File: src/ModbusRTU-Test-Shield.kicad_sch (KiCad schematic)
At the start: 23 parts, among them J1 Conn_01x08_UNO_Digital_1, J2 Conn_01x10_UNO_Digital_2, J3 Conn_01x08_UNO_Power, J4 Conn_01x06_UNO_Analog, J5 Screw_Terminal_01x03, SW1 SW_Push, SW2 SW_Push, SW3 SW_Push, SW4 SW_DPDT_x2, U1 LT1785AxN8

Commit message: Completed first draft.
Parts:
- removed R6: 2K, Resistor_THT:R_Axial_DIN0207_L6.3mm_D2.5mm_P10.16mm_Horizontal, symbol Device:R
- added D5: YEL, LED_THT:LED_D3.0mm, symbol Device:LED
- added R5: 330, Resistor_THT:R_Axial_DIN0207_L6.3mm_D2.5mm_P10.16mm_Horizontal, symbol Device:R
- added R7: 2K, Resistor_THT:R_Axial_DIN0207_L6.3mm_D2.5mm_P10.16mm_Horizontal, symbol Device:R
- renumbered R5 to R6
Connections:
- net *5: now also R1.1; no longer D1.2 (A)
- net *6: now also R2.1; no longer D2.2 (A)
- net 13: now also R5.1
- net 7: now also R3.1; no longer D3.2 (A)
- net 8: now also R4.1; no longer D4.2 (A)
- net GND: now also D1.1 (K), D2.1 (K), D3.1 (K), D4.1 (K), D5.1 (K), R7.2; no longer R1.2, R2.2, R3.2, R4.2
- net at R6.2, SW4.5 (B): now also R7.1
- new net: D1.2 (A), R1.2
- new net: D4.2 (A), R4.2
- new net: D2.2 (A), R2.2
- new net: D5.2 (A), R5.2
- new net: D3.2 (A), R3.2
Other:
- moved on the sheet: C1, D1, D2, D3, D4, J1, J2, J3, J4, J5, R1, R2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

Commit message: Added RS-232 on an RJ12 connector. Completed second draft.
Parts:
- added C2, C3, C4, C5, C6: 1uF, Capacitor_THT:CP_Radial_D5.0mm_P2.50mm, symbol Device:C_Polarized_Small
- added D10, D9: YEL, LED_THT:LED_D3.0mm, symbol Device:LED
- added D11: D_Schottky, Diode_THT:D_DO-41_SOD81_P10.16mm_Horizontal, symbol Device:D_Schottky
- added D6, D7: D_Schottky, Diode_THT:D_DO-35_SOD27_P7.62mm_Horizontal, symbol Device:D_Schottky
- added D8: GRN, LED_THT:LED_D3.0mm, symbol Device:LED
- added J6: 6P6C, Connector_RJ:RJ12_Amphenol_54601, symbol Connector:6P6C
- added R8, R9: 330, Resistor_THT:R_Axial_DIN0207_L6.3mm_D2.5mm_P10.16mm_Horizontal, symbol Device:R
- added U2: MAX232, Package_DIP:DIP-16_W7.62mm, symbol Interface_UART:MAX232
- R6: value 1K -> 10K
- R7: value 2K -> 330
- SW1: value SW_Push -> RESET; footprint Button_Switch_THT:SW_PUSH_6mm -> Project_Footprints:SW_PUSH_6mm_Reset
- SW2: value SW_Push -> BUTTON1
- SW3: value SW_Push -> BUTTON2
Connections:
- net +5V: now also C6.1, D11.1 (K), D8.2 (A), J6.2, U2.16 (VCC)
- net GND: now also C4.2, C5.1, C6.2, J6.1, J6.6, U2.15 (GND)
- net IOREF: now also R6.1, D10.2 (A), D9.2 (A)
- net at U1.1 (RO): now also D6.1 (K); no longer R6.1
- net RX: now reaches SW4.2 (B)
- net RX: now also R6.2, D6.2 (A), D7.2 (A), R9.2; no longer U1.4 (DI)
- net RS485_D+: now reaches J5.1 (Pin_1), U1.6 (A)
- net RS485_D-: now reaches J5.2 (Pin_2), U1.7 (B)
- net RESET: now reaches J3.3 (RESET), SW1.1
- net *10 renamed SOFT_RX
- net SOFT_RX: now also SW4.3 (C); no longer SW4.6 (C)
- net *11 renamed SOFT_TX
- net SOFT_TX: now also SW4.6 (C); no longer SW4.3 (C)
- net *3 renamed BUTTON1
- net *5 renamed LED4
- net *6 renamed LED3
- net 13 renamed DE
- net 2 renamed BUTTON2
- net 7 renamed LED2
- net 8 renamed LED1
- net A0 renamed POT1
- net A1 renamed POT2
- net RX/0 renamed HARD_RX
- net HARD_RX: now also SW4.1 (A); no longer SW4.4 (A)
- net TX/1 renamed HARD_TX
- net HARD_TX: now also SW4.4 (A); no longer SW4.1 (A)
- new net: D10.1 (K), R9.1
- new net: C3.1, U2.1 (C1+)
- new net: C3.2, U2.3 (C1-)
- new net: D9.1 (K), R8.1
- new net: C5.2, U2.6 (VS-)
- new net: D8.1 (K), R7.1
- new net: D11.2 (A), J6.5
- new net: D7.1 (K), U2.12 (R1OUT)
- new net: C4.1, U2.2 (VS+)
- new net: C2.1, U2.4 (C2+)
- new net: C2.2, U2.5 (C2-)
- new net RS232_RX: J6.3, U2.13 (R1IN)
- new net RS232_TX: J6.4, U2.14 (T1OUT)
- new net TX: R8.2, SW4.5 (B), U1.4 (DI), U2.11 (T1IN)
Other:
- note removed: "* Indicates a PWM-capable pin"
- moved on the sheet: C1, D5, J5, R5, RV1, RV2, SW1, SW2, SW3

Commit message: Added some 3D models. Created project footprints for RJ12 and screw terminal connectors. Placed and locked RJ12 and screw terminal connector.
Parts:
- J5: footprint Connector_Phoenix_MC:PhoenixContact_MC_1,5_3-G-3.5_1x03_P3.50mm_Horizontal -> Project_Footprints:PhoenixContact_BCH-350H-3_RS485; Manufacturer (none) -> Phoenix Contact; Part Number (none) -> 5430438
- J6: footprint Connector_RJ:RJ12_Amphenol_54601 -> Project_Footprints:FCI_54601-906WPLF; Manufacturer (none) -> Amphenol ICC (FCI); Part Number (none) -> 54601-906WPLF
- R1, R2, R3, R4, R5, R6, R7, R8, R9: footprint Resistor_THT:R_Axial_DIN0207_L6.3mm_D2.5mm_P10.16mm_Horizontal -> Resistor_THT:R_Axial_DIN0204_L3.6mm_D1.6mm_P7.62mm_Horizontal
- U1: footprint Package_DIP:DIP-8_W7.62mm -> Package_DIP:DIP-8_W7.62mm_Socket
- U2: footprint Package_DIP:DIP-16_W7.62mm -> Package_DIP:DIP-16_W7.62mm_Socket
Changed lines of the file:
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@@
       (effects (font (size 1.27 1.27)) (justify left))
     )
-    (property "Footprint" "Resistor_THT:R_Axial_DIN0207_L6.3mm_D2.5mm_P10.16mm_Horizontal" (at 430.022 105.41 90)
+    (property "Footprint" "Resistor_THT:R_Axial_DIN0204_L3.6mm_D1.6mm_P7.62mm_Horizontal" (at 430.022 105.41 90)
       (effects (font (size 1.27 1.27)) hide)
     )
@@
       (effects (font (size 1.27 1.27)) (justify left))
     )
-    (property "Footprint" "Package_DIP:DIP-8_W7.62mm" (at 165.1 182.88 0)
+    (property "Footprint" "Package_DIP:DIP-8_W7.62mm_Socket" (at 165.1 182.88 0)
       (effects (font (size 1.27 1.27)) hide)
     )
     (property "Datasheet" "https://www.analog.com/media/en/technical-documentation/data-sheets/LT1785-1785A-1791-1791A.pdf" (at 177.8 157.48 0)
+      (effects (font (size 1.27 1.27)) hide)
+    )
+    (property "Manufacturer" "" (at 165.1 160.02 0)
+      (effects (font (size 1.27 1.27)) hide)
+    )
+    (property "Part Number" "" (at 165.1 160.02 0)
+      (effects (font (size 1.27 1.27)) hide)
+    )
+    (property "Description" "" (at 165.1 160.02 0)
+      (effects (font (size 1.27 1.27)) hide)
+    )
+    (property "Item" "" (at 165.1 160.02 0)
       (effects (font (size 1.27 1.27)) hide)
     )
@@
       (effects (font (size 1.27 1.27)) (justify left))
     )
-    (property "Footprint" "Resistor_THT:R_Axial_DIN0207_L6.3mm_D2.5mm_P10.16mm_Horizontal" (at 417.322 105.41 90)
+    (property "Footprint" "Resistor_THT:R_Axial_DIN0204_L3.6mm_D1.6mm_P7.62mm_Horizontal" (at 417.322 105.41 90)
       (effects (font (size 1.27 1.27)) hide)
     )
@@
       (effects (font (size 1.27 1.27)) (justify left))
     )
-    (property "Footprint" "Resistor_THT:R_Axial_DIN0207_L6.3mm_D2.5mm_P10.16mm_Horizontal" (at 353.822 95.25 90)
+    (property "Footprint" "Resistor_THT:R_Axial_DIN0204_L3.6mm_D1.6mm_P7.62mm_Horizontal" (at 353.822 95.25 90)
       (effects (font (size 1.27 1.27)) hide)
     )
@@
       (effects (font (size 1.27 1.27)) (justify left))
     )
-    (property "Footprint" "Resistor_THT:R_Axial_DIN0207_L6.3mm_D2.5mm_P10.16mm_Horizontal" (at 341.122 95.25 90)
+    (property "Footprint" "Resistor_THT:R_Axial_DIN0204_L3.6mm_D1.6mm_P7.62mm_Horizontal" (at 341.122 95.25 90)
       (effects (font (size 1.27 1.27)) hide)
     )
@@
       (effects (font (size 1.27 1.27)) (justify left))
     )
-    (property "Footprint" "Connector_Phoenix_MC:PhoenixContact_MC_1,5_3-G-3.5_1x03_P3.50mm_Horizontal" (at 106.68 154.94 0)
-      (effects (font (size 1.27 1.27)) hide)
-    )
-    (property "Datasheet" "~" (at 106.68 154.94 0)
+    (property "Footprint" "Project_Footprints:PhoenixContact_BCH-350H-3_RS485" (at 106.68 154.94 0)
+      (effects (font (size 1.27 1.27)) hide)
+    )
+    (property "Datasheet" "https://pxc-crisp-production-platform-cr-s3downloadbucket-1rf23da6xdlmt.s3.eu-west-1.amazonaws.com/8023209?response-content-disposition=inline%3B%20filename%3D%22pxc_5430438_01_01_BCH-350H-3-GY_FAM.pdf%22&X-Amz-Algorithm=AWS4-HMAC-SHA256&X-Amz-Date=20231214T042124Z&X-Amz-SignedHeaders=host&X-Amz-Expires=10800&X-Amz-Credential=AKIAWWXX4BDRFPQUJUER%2F20231214%2Feu-west-1%2Fs3%2Faws4_request&X-Amz-Signature=642cf48a3280ba600a0d77ac701bfd69076ef8d12d5102349e7adfa4ea6ee9f3" (at 106.68 154.94 0)
+      (effects (font (size 1.27 1.27)) hide)
+    )
+    (property "Manufacturer" "Phoenix Contact" (at 106.68 154.94 0)
+      (effects (font (size 1.27 1.27)) hide)
+    )
+    (property "Part Number" "5430438" (at 106.68 154.94 0)
+      (effects (font (size 1.27 1.27)) hide)
+    )
+    (property "Description" "3-Position Terminal Block Header" (at 106.68 154.94 0)
+      (effects (font (size 1.27 1.27)) hide)
+    )
+    (property "Item" "" (at 106.68 154.94 0)
       (effects (font (size 1.27 1.27)) hide)
     )
@@
       (effects (font (size 1.27 1.27)) (justify left))
     )
-    (property "Footprint" "Resistor_THT:R_Axial_DIN0207_L6.3mm_D2.5mm_P10.16mm_Horizontal" (at 404.622 105.41 90)
+    (property "Footprint" "Resistor_THT:R_Axial_DIN0204_L3.6mm_D1.6mm_P7.62mm_Horizontal" (at 404.622 105.41 90)
       (effects (font (size 1.27 1.27)) hide)
     )
@@
       (effects (font (size 1.27 1.27)) (justify left))
     )
-    (property "Footprint" "Resistor_THT:R_Axial_DIN0207_L6.3mm_D2.5mm_P10.16mm_Horizontal" (at 239.522 184.15 90)
+    (property "Footprint" "Resistor_THT:R_Axial_DIN0204_L3.6mm_D1.6mm_P7.62mm_Horizontal" (at 239.522 184.15 90)
       (effects (font (size 1.27 1.27)) hide)
     )
@@
       (effects (font (size 1.27 1.27)) (justify left))
     )
-    (property "Footprint" "Resistor_THT:R_Axial_DIN0207_L6.3mm_D2.5mm_P10.16mm_Horizontal" (at 366.522 95.25 90)
+    (property "Footprint" "Resistor_THT:R_Axial_DIN0204_L3.6mm_D1.6mm_P7.62mm_Horizontal" (at 366.522 95.25 90)
       (effects (font (size 1.27 1.27)) hide)
     )
@@
       (effects (font (size 1.27 1.27)) (justify right))
     )
-    (property "Footprint" "Connector_RJ:RJ12_Amphenol_54601" (at 50.8 221.615 90)
-      (effects (font (size 1.27 1.27)) hide)
-    )
-    (property "Datasheet" "~" (at 50.8 221.615 90)
+    (property "Footprint" "Project_Footprints:FCI_54601-906WPLF" (at 50.8 221.615 90)
+      (effects (font (size 1.27 1.27)) hide)
+    )
+    (property "Datasheet" "https://cdn.amphenol-cs.com/media/wysiwyg/files/drawing/c-bmj-0082.pdf" (at 50.8 221.615 90)
+      (effects (font (size 1.27 1.27)) hide)
+    )
+    (property "Manufacturer" "Amphenol ICC (FCI)" (at 50.8 220.98 0)
+      (effects (font (size 1.27 1.27)) hide)
+    )
+    (property "Part Number" "54601-906WPLF" (at 50.8 220.98 0)
+      (effects (font (size 1.27 1.27)) hide)
+    )
+    (property "Description" "RJ12 Connector" (at 50.8 220.98 0)
+      (effects (font (size 1.27 1.27)) hide)
+    )
+    (property "Item" "" (at 50.8 220.98 0)
       (effects (font (size 1.27 1.27)) hide)
     )
@@
       (effects (font (size 1.27 1.27)) (justify left))
     )
-    (property "Footprint" "Resistor_THT:R_Axial_DIN0207_L6.3mm_D2.5mm_P10.16mm_Horizontal" (at 379.222 95.25 90)
+    (property "Footprint" "Resistor_THT:R_Axial_DIN0204_L3.6mm_D1.6mm_P7.62mm_Horizontal" (at 379.222 95.25 90)
       (effects (font (size 1.27 1.27)) hide)
     )
@@
       (effects (font (size 1.27 1.27)) (justify left))
     )
-    (property "Footprint" "Package_DIP:DIP-16_W7.62mm" (at 214.63 318.77 0)
+    (property "Footprint" "Package_DIP:DIP-16_W7.62mm_Socket" (at 214.63 318.77 0)
       (effects (font (size 1.27 1.27)) (justify left) hide)
     )
     (property "Datasheet" "http://www.ti.com/lit/ds/symlink/max232.pdf" (at 215.9 289.56 0)
+      (effects (font (size 1.27 1.27)) hide)
+    )
+    (property "Manufacturer" "" (at 215.9 292.1 0)
+      (effects (font (size 1.27 1.27)) hide)
+    )
+    (property "Part Number" "" (at 215.9 292.1 0)
+      (effects (font (size 1.27 1.27)) hide)
+    )
+    (property "Description" "" (at 215.9 292.1 0)
+      (effects (font (size 1.27 1.27)) hide)
+    )
+    (property "Item" "" (at 215.9 292.1 0)
       (effects (font (size 1.27 1.27)) hide)
     )
@@
       (effects (font (size 1.27 1.27)) (justify left))
     )
-    (property "Footprint" "Resistor_THT:R_Axial_DIN0207_L6.3mm_D2.5mm_P10.16mm_Horizontal" (at 391.922 95.25 90)
-      (effects (font (size 1.27 1.27)) hide)
-    )
+    (property "Footprint" "Resistor_THT:R_Axial_DIN0204_L3.6mm_D1.6mm_P7.62mm_Horizontal" (at 391.922 95.25 90)
+      (effects (font (size 1.27 1.27)) hide)
+    )

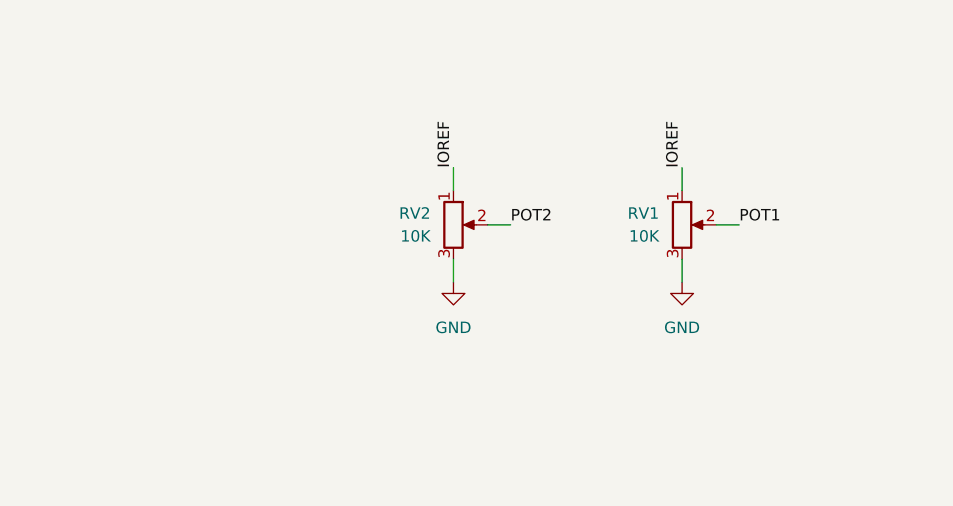
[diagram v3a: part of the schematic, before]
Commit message: Refined button footprints. Updated and refined potentiometer footprints and models.
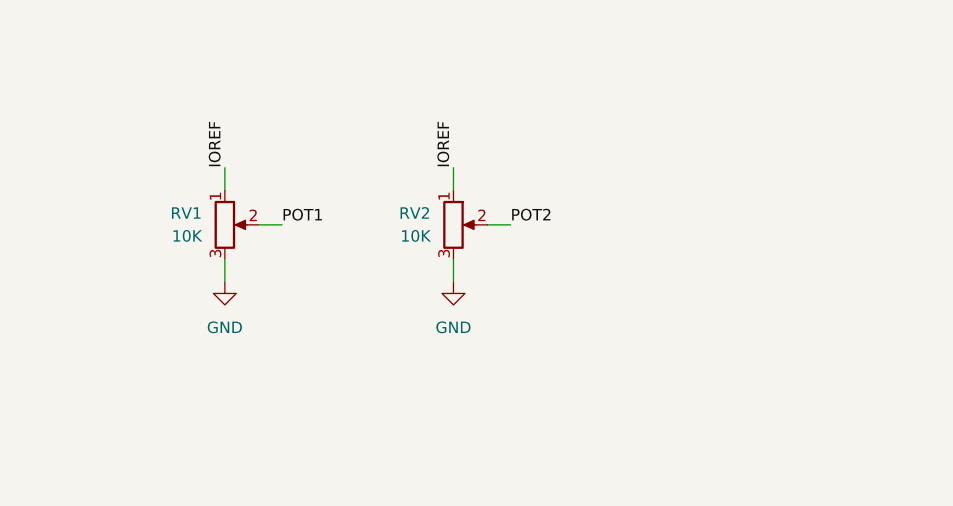
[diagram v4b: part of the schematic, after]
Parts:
- RV1: footprint Potentiometer_THT:Potentiometer_ACP_CA9-V10_Vertical -> Project_Footprints:Potentiometer_Piher_PT-10-V10_Vertical; Label (none) -> POT 1; Manufacturer (none) -> Amphenol Piher Sensing Systems; Part Number (none) -> PT10MV10-103A2020-E-S
- RV2: footprint Potentiometer_THT:Potentiometer_ACP_CA9-V10_Vertical -> Project_Footprints:Potentiometer_Piher_PT-10-V10_Vertical; Label (none) -> POT 2; Manufacturer (none) -> Amphenol Piher Sensing Systems; Part Number (none) -> PT10MV10-103A2020-E-S
- SW1: footprint Project_Footprints:SW_PUSH_6mm_Reset -> Project_Footprints:SW_PUSH_6mm; Label (none) -> RESET
- SW2: footprint Button_Switch_THT:SW_PUSH_6mm -> Project_Footprints:SW_PUSH_6mm; Label (none) -> BUTTON 1
- SW3: footprint Button_Switch_THT:SW_PUSH_6mm -> Project_Footprints:SW_PUSH_6mm; Label (none) -> BUTTON 2
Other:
- moved on the sheet: RV1
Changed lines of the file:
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@@
     (stroke (width 0) (type solid))
   )
-  (wire (pts (xy 127 50.8) (xy 127 53.34))
+  (wire (pts (xy 76.2 50.8) (xy 76.2 53.34))
     (stroke (width 0) (type default))
   )
@@
     (stroke (width 0) (type default))
   )
-  (wire (pts (xy 130.81 57.15) (xy 133.35 57.15))
+  (wire (pts (xy 80.01 57.15) (xy 82.55 57.15))
     (stroke (width 0) (type default))
   )
@@
     (stroke (width 0) (type solid))
   )
-  (wire (pts (xy 127 60.96) (xy 127 63.5))
+  (wire (pts (xy 76.2 60.96) (xy 76.2 63.5))
     (stroke (width 0) (type default))
   )
@@
     (effects (font (size 1.27 1.27)) (justify left bottom))
   )
-  (label "IOREF" (at 127 50.8 90) (fields_autoplaced)
+  (label "IOREF" (at 76.2 50.8 90) (fields_autoplaced)
     (effects (font (size 1.27 1.27)) (justify left bottom))
   )
@@
     (effects (font (size 1.27 1.27)) (justify left bottom))
   )
-  (label "POT1" (at 133.35 57.15 0) (fields_autoplaced)
+  (label "POT1" (at 82.55 57.15 0) (fields_autoplaced)
     (effects (font (size 1.27 1.27)) (justify left bottom))
   )
@@
     )
   )
-  (symbol (lib_name "GND_1") (lib_id "power:GND") (at 127 63.5 0) (unit 1)
-    (in_bom yes) (on_board yes) (dnp no) (fields_autoplaced)
-    (property "Reference" "#PWR07" (at 127 69.85 0)
-      (effects (font (size 1.27 1.27)) hide)
-    )
-    (property "Value" "GND" (at 127 68.58 0)
-      (effects (font (size 1.27 1.27)))
-    )
-    (property "Footprint" "" (at 127 63.5 0)
-      (effects (font (size 1.27 1.27)) hide)
-    )
-    (property "Datasheet" "" (at 127 63.5 0)
+  (symbol (lib_name "GND_1") (lib_id "power:GND") (at 76.2 63.5 0) (unit 1)
+    (in_bom yes) (on_board yes) (dnp no) (fields_autoplaced)
+    (property "Reference" "#PWR07" (at 76.2 69.85 0)
+      (effects (font (size 1.27 1.27)) hide)
+    )
+    (property "Value" "GND" (at 76.2 68.58 0)
+      (effects (font (size 1.27 1.27)))
+    )
+    (property "Footprint" "" (at 76.2 63.5 0)
+      (effects (font (size 1.27 1.27)) hide)
+    )
+    (property "Datasheet" "" (at 76.2 63.5 0)
       (effects (font (size 1.27 1.27)) hide)
     )
@@
       (effects (font (size 1.27 1.27)) (justify left))
     )
-    (property "Footprint" "Button_Switch_THT:SW_PUSH_6mm" (at 314.96 101.6 0)
+    (property "Footprint" "Project_Footprints:SW_PUSH_6mm" (at 314.96 101.6 0)
       (effects (font (size 1.27 1.27)) hide)
     )
@@
       (effects (font (size 1.27 1.27)) hide)
     )
+    (property "Manufacturer" "" (at 309.88 101.6 0)
+      (effects (font (size 1.27 1.27)) hide)
+    )
+    (property "Part Number" "" (at 309.88 101.6 0)
+      (effects (font (size 1.27 1.27)) hide)
+    )
+    (property "Description" "" (at 309.88 101.6 0)
+      (effects (font (size 1.27 1.27)) hide)
+    )
+    (property "Item" "" (at 309.88 101.6 0)
+      (effects (font (size 1.27 1.27)) hide)
+    )
+    (property "Label" "BUTTON 1" (at 309.88 101.6 90)
+      (effects (font (size 1.27 1.27)) hide)
+    )
     (pin "1")
     (pin "2")
@@
       (effects (font (size 1.27 1.27)) (justify left))
     )
-    (property "Footprint" "Button_Switch_THT:SW_PUSH_6mm" (at 330.2 101.6 0)
+    (property "Footprint" "Project_Footprints:SW_PUSH_6mm" (at 330.2 101.6 0)
       (effects (font (size 1.27 1.27)) hide)
     )
     (property "Datasheet" "~" (at 330.2 101.6 0)
+      (effects (font (size 1.27 1.27)) hide)
+    )
+    (property "Manufacturer" "" (at 325.12 101.6 0)
+      (effects (font (size 1.27 1.27)) hide)
+    )
+    (property "Part Number" "" (at 325.12 101.6 0)
+      (effects (font (size 1.27 1.27)) hide)
+    )
+    (property "Description" "" (at 325.12 101.6 0)
+      (effects (font (size 1.27 1.27)) hide)
+    )
+    (property "Item" "" (at 325.12 101.6 0)
+      (effects (font (size 1.27 1.27)) hide)
+    )
+    (property "Label" "BUTTON 2" (at 325.12 101.6 90)
       (effects (font (size 1.27 1.27)) hide)
     )
@@
       (effects (font (size 1.27 1.27)) (justify left))
     )
-    (property "Footprint" "Project_Footprints:SW_PUSH_6mm_Reset" (at 299.72 101.6 0)
+    (property "Footprint" "Project_Footprints:SW_PUSH_6mm" (at 299.72 101.6 0)
       (effects (font (size 1.27 1.27)) hide)
     )
@@
       (effects (font (size 1.27 1.27)) hide)
     )
+    (property "Manufacturer" "" (at 294.64 101.6 0)
+      (effects (font (size 1.27 1.27)) hide)
+    )
+    (property "Part Number" "" (at 294.64 101.6 0)
+      (effects (font (size 1.27 1.27)) hide)
+    )
+    (property "Description" "" (at 294.64 101.6 0)
+      (effects (font (size 1.27 1.27)) hide)
+    )
+    (property "Item" "" (at 294.64 101.6 0)
+      (effects (font (size 1.27 1.27)) hide)
+    )
+    (property "Label" "RESET" (at 294.64 101.6 90)
+      (effects (font (size 1.27 1.27)) hide)
+    )
     (pin "1")
     (pin "2")
@@
     )
   )
-  (symbol (lib_id "Device:R_Potentiometer") (at 127 57.15 0) (unit 1)
-    (in_bom yes) (on_board yes) (dnp no) (fields_autoplaced)
-    (property "Reference" "RV1" (at 124.46 55.88 0)
-      (effects (font (size 1.27 1.27)) (justify right))
-    )
-    (property "Value" "10K" (at 124.46 58.42 0)
-      (effects (font (size 1.27 1.27)) (justify right))
-    )
-    (property "Footprint" "Potentiometer_THT:Potentiometer_ACP_CA9-V10_Vertical" (at 127 57.15 0)
-      (effects (font (size 1.27 1.27)) hide)
-    )
-    (property "Datasheet" "~" (at 127 57.15 0)
+  (symbol (lib_id "Device:R_Potentiometer") (at 76.2 57.15 0) (unit 1)
+    (in_bom yes) (on_board yes) (dnp no) (fields_autoplaced)
+    (property "Reference" "RV1" (at 73.66 55.88 0)
+      (effects (font (size 1.27 1.27)) (justify right))
+    )
+    (property "Value" "10K" (at 73.66 58.42 0)
+      (effects (font (size 1.27 1.27)) (justify right))
+    )
+    (property "Footprint" "Project_Footprints:Potentiometer_Piher_PT-10-V10_Vertical" (at 76.2 57.15 0)
+      (effects (font (size 1.27 1.27)) hide)
+    )
+    (property "Datasheet" "https://www.piher.net/wp-content/uploads/PIHER_PT-10_PTC-10.pdf" (at 76.2 57.15 0)
+      (effects (font (size 1.27 1.27)) hide)
+    )
+    (property "Manufacturer" "Amphenol Piher Sensing Systems" (at 76.2 57.15 0)
+      (effects (font (size 1.27 1.27)) hide)
+    )
+    (property "Part Number" "PT10MV10-103A2020-E-S" (at 76.2 57.15 0)
+      (effects (font (size 1.27 1.27)) hide)
+    )
+    (property "Description" "10K Ohm Potentiometer" (at 76.2 57.15 0)
+      (effects (font (size 1.27 1.27)) hide)
+    )
+    (property "Item" "" (at 76.2 57.15 0)
+      (effects (font (size 1.27 1.27)) hide)
+    )
+    (property "Label" "POT 1" (at 76.2 57.15 0)
       (effects (font (size 1.27 1.27)) hide)
     )
@@
       (effects (font (size 1.27 1.27)) (justify right))
     )
-    (property "Footprint" "Potentiometer_THT:Potentiometer_ACP_CA9-V10_Vertical" (at 101.6 57.15 0)
-      (effects (font (size 1.27 1.27)) hide)
-    )
-    (property "Datasheet" "~" (at 101.6 57.15 0)
-      (effects (font (size 1.27 1.27)) hide)
-    )
+    (property "Footprint" "Project_Footprints:Potentiometer_Piher_PT-10-V10_Vertical" (at 101.6 57.15 0)
+      (effects (font (size 1.27 1.27)) hide)
+    )
+    (property "Datasheet" "https://www.piher.net/wp-content/uploads/PIHER_PT-10_PTC-10.pdf" (at 101.6 57.15 0)
+      (effects (font (size 1.27 1.27)) hide)
+    )
+    (property "Manufacturer" "Amphenol Piher Sensing Systems" (at 101.6 57.15 0)
+      (effects (font (size 1.27 1.27)) hide)
+    )
+    (property "Part Number" "PT10MV10-103A2020-E-S" (at 101.6 57.15 0)
+      (effects (font (size 1.27 1.27)) hide)
+    )
+    (property "Description" "10K Ohm Potentiometer" (at 101.6 57.15 0)
+      (effects (font (size 1.27 1.27)) hide)
+    )
+    (property "Item" "" (at 101.6 57.15 0)
+      (effects (font (size 1.27 1.27)) hide)
+    )
+    (property "Label" "POT 2" (at 101.6 57.15 0)
+      (effects (font (size 1.27 1.27)) hide)
+    )
